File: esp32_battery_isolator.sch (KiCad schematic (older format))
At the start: 83 parts, among them J1 BATT1, J2 Conn_01x04_Female, J3 USB_B_Micro, J4 BATT2, J5 LOAD1, J6 CHGR, J7 LOAD2, J8 LOAD3, J9 Conn_01x03_Male, Q1 MMBT3904, Q10 AONR21321, Q11 AONR21321, Q12 MMBT3904, Q13 AONR21321, Q2 AONR21321, Q3 MMBT3904, Q4 AONR21321, Q5 MMBT3904, Q6 AONR21321, Q7 MMBT3904, Q8 AONR21321, Q9 MMBT3904, SW1 C492887, SW2 C492887, U1 ESP32-WROOM-32D, U2 XL1509_SOP8, U3 ADC128D818, U4 CC6903SO-30A, U5 CH340N, U6 CC6903SO-30A

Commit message: closer
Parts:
- removed Q13, Q6: AONR21321, Acea:DFN-TRANS_AONR21321, symbol Transistor_FET:QM6015D
- removed Q5: MMBT3904, Package_TO_SOT_SMD:SOT-23, symbol Transistor_BJT:MMBT3904
- removed R15: 200k, Resistor_SMD:R_0603_1608Metric, symbol Device:R_Small
- removed R25: 11k, Resistor_SMD:R_0603_1608Metric, symbol Device:R_Small
- removed R29: 510R, Resistor_SMD:R_0603_1608Metric, symbol Device:R_Small
- added BZ1: Buzzer, Buzzer_Beeper:SMDBuzzer_C201046, symbol Device:Buzzer
- Q10, Q11, Q2, Q4, Q8: value AONR21321 -> AONR21357
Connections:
- net B2C is gone; now on net COM: J9.1 (Pin_1), Q10.S, Q2.S, Q8.S, U6.3 (IP-), U6.4 (IP-)
- net B1VM: no longer R14.1
- net B2VM: no longer R16.1, R17.1, R20.1
- net COM: now also R14.1, R16.1, R17.1, R20.1
- net GND: now also BZ1.1 (-)
- net RST: now also U5.4 (~RTS)
- net BZR: now reaches U1.30 (IO18)
- net BZR: now also BZ1.2 (+)
- net B2ON: no longer names the net of U1.10 (IO25)
- no-connect marks 24 -> 23
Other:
- note added: "18V max."
- note added: "20A max cont.\n66A pulsed"
- note added: "25A max."
- note added: "2A max."
- note added: "3.4V max."
- note added: "Batt 2 connection (auxiliary)"
- note added: "Buzzer"
- note added: "CLRs?"
- note added: "Flyback?"
- note added: "Hold boot button to enter bootloader \nas ~RST~ will reset the uC automatically"
- note added: "Load 1 (freezer)"
- note added: "Load 2 (fridge)"
- note added: "Load 3 (lights)"
- note removed: "B1VM will only have 12v when B1 is \nconnected, threfore, B1’s MOSFETs will \nconduct without B1 attached."
- note removed: "B2VM will only have 12v when B2 is \nconnected, threfore, B2s MOSFETs will \nconduct without B2 attached."
- note removed: "Batt 2 isolator (auxiliary)"
- note removed: "Load 1 (fridge?)"
- note removed: "Load 2 (freezer?)"
- note removed: "Load 3 (lights?)"
- moved on the sheet: C10, C9, J1, J4, J6, Q1, Q11, Q4, R14, R27, R5, U4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

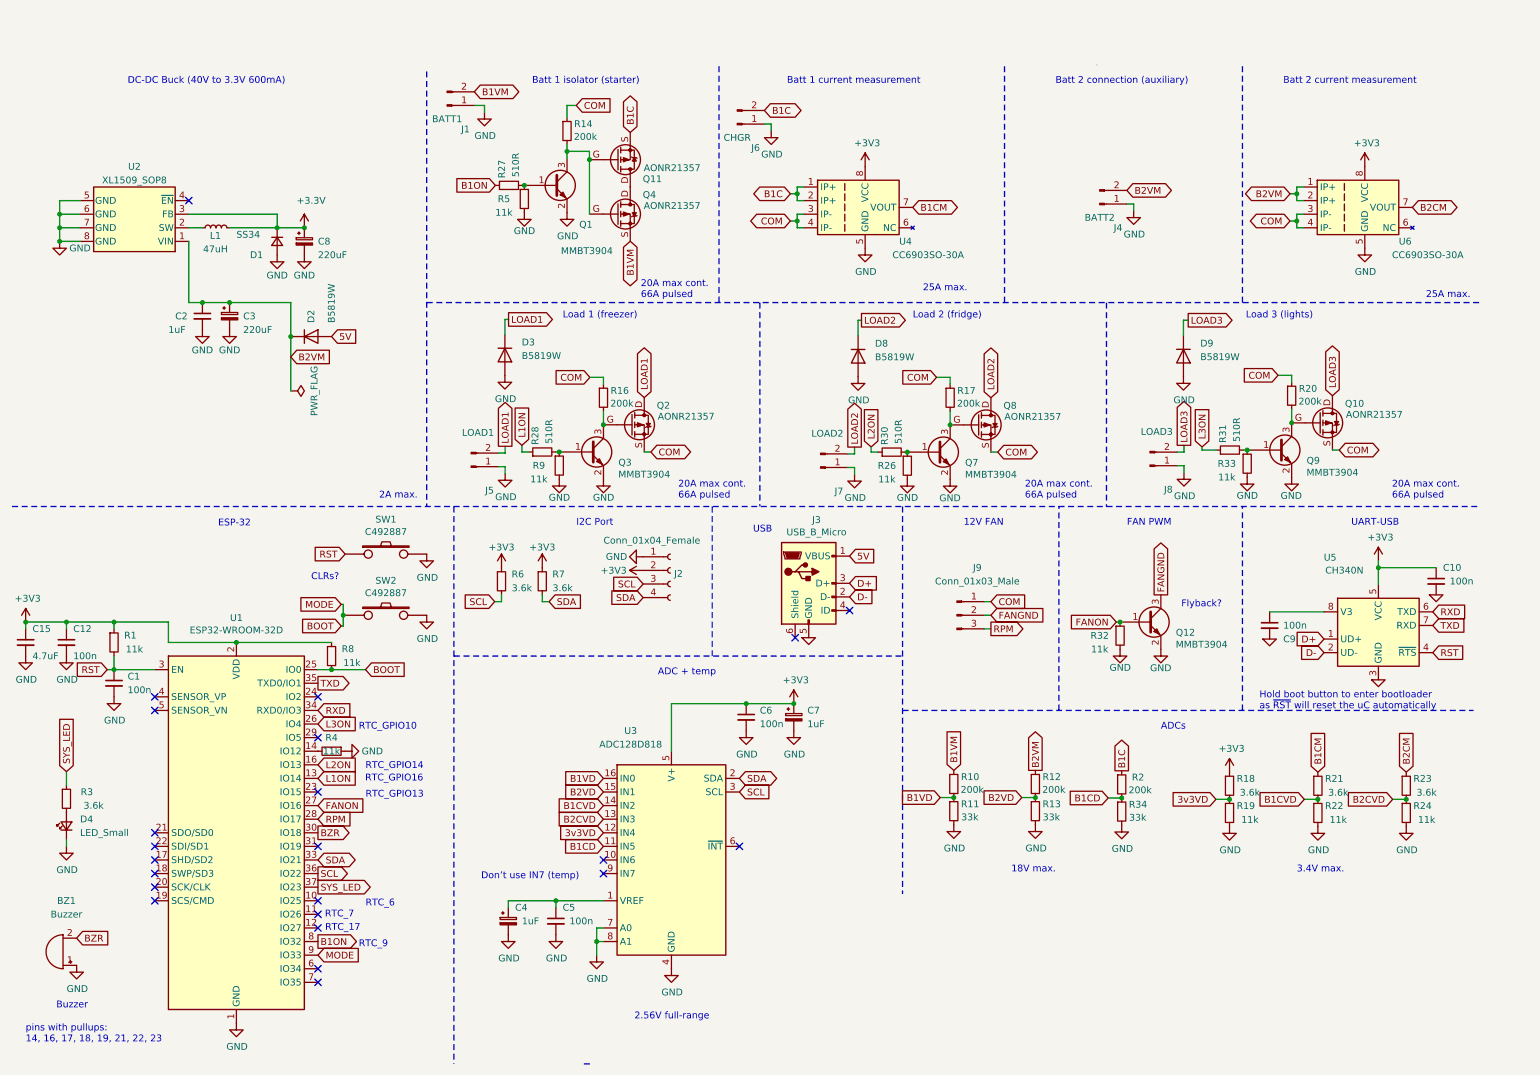
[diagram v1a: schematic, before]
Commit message: fixed daily couters not resetting
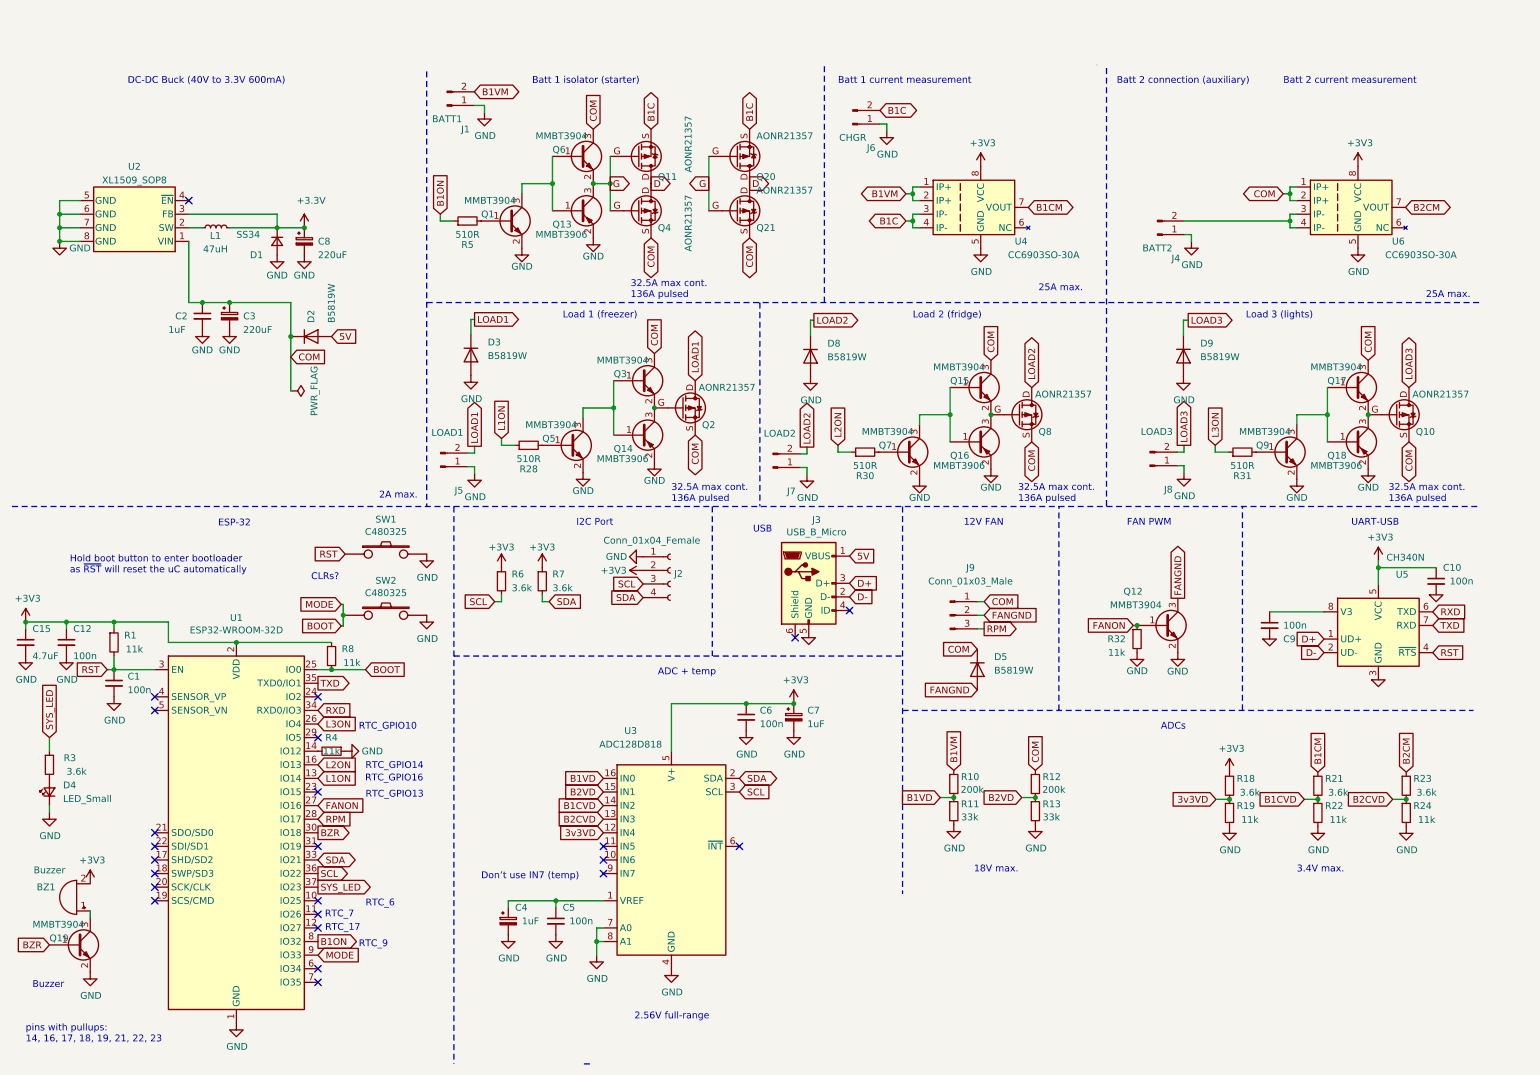
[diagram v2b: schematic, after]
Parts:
- removed R14, R16, R17, R2, R20: 200k, Resistor_SMD:R_0603_1608Metric, symbol Device:R_Small
- removed R26, R33, R9: 11k, Resistor_SMD:R_0603_1608Metric, symbol Device:R_Small
- removed R27: 510R, Resistor_SMD:R_0603_1608Metric, symbol Device:R_Small
- removed R34: 33k, Resistor_SMD:R_0603_1608Metric, symbol Device:R_Small
- added D5: B5819W, Diode_SMD:D_SOD-123, symbol Diode:1N4148WS
- added Q13, Q14, Q16, Q18: MMBT3906, Package_TO_SOT_SMD:SOT-23, symbol Transistor_BJT:MMBT3906
- added Q15, Q17, Q19, Q5, Q6: MMBT3904, Package_TO_SOT_SMD:SOT-23, symbol Transistor_BJT:MMBT3904
- added Q20, Q21: AONR21357, Acea:DFN-TRANS_AONR21321, symbol Transistor_FET:QM6015D
- R5: value 11k -> 510R; lcsc_part_number C25950 -> C269885; lcsc_url https://lcsc.com/product-detail/Chip-Resistor-Surface-Mount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 -> (none)
- SW1, SW2: value C492887 -> C480325; lcsc_part_number C492887 -> C480325; mfr_part_number TS-1091S-A5B3-C1D2 -> (none)
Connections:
- net +3V3: now also BZ1.2 (+)
- net B1C: now also U4.3 (IP-), U4.4 (IP-), Q20.S; no longer U4.1 (IP+), U4.2 (IP+)
- net B1ON: now also R5.1
- net B1VM: now also U4.1 (IP+), U4.2 (IP+); no longer Q4.S
- net BZR: now also Q19.1 (B); no longer BZ1.2 (+)
- net COM: now also C2.1, C3.1, D2.1 (K), Q3.3 (C), Q4.S, R12.1, U2.1 (VIN), U6.1 (IP+), U6.2 (IP+), D5.1 (K), Q15.3 (C), Q17.3 (C), Q21.S, Q6.3 (C); no longer U4.3 (IP-), U4.4 (IP-), U6.3 (IP-), U6.4 (IP-)
- net FANGND: now also D5.2 (A)
- net GND: now also Q13.2 (E), Q14.2 (E), Q16.2 (E), Q18.2 (E), Q19.2 (E), Q5.2 (E); no longer BZ1.1 (-), Q3.2 (E), R5.2
- net G: now reaches Q11.G, Q4.G
- net G: now also Q13.3 (C), Q20.G, Q21.G, Q6.2 (E); no longer Q1.3 (C)
- net at Q9.3 (C): now also Q17.1 (B), Q18.1 (B); no longer Q10.G
- net at Q7.3 (C): now also Q15.1 (B), Q16.1 (B); no longer Q8.G
- net at Q2.G: now also Q3.2 (E), Q14.3 (C); no longer Q3.3 (C)
- net at Q1.1 (B): now also R5.2; no longer R5.1
- net at Q3.1 (B): now also Q14.1 (B), Q5.3 (C); no longer R28.2
- net D: now reaches Q11.D, Q4.D
- net D: now also Q20.D, Q21.D
- net B1CD: no longer names the net of U3.11 (IN5)
- removed net B2VM: C2.1, C3.1, D2.1 (K), J4.2 (Pin_2), R12.1, U2.1 (VIN), U6.1 (IP+), U6.2 (IP+)
- new net: J4.2 (Pin_2), U6.3 (IP-), U6.4 (IP-)
- new net: BZ1.1 (-), Q19.3 (C)
- new net: Q1.3 (C), Q13.1 (B), Q6.1 (B)
- new net: Q5.1 (B), R28.2
- new net: Q15.2 (E), Q16.3 (C), Q8.G
- new net: Q10.G, Q17.2 (E), Q18.3 (C)
- no-connect marks 23 -> 24
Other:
- note added: "32.5A max cont.\n136A pulsed"
- note removed: "20A max cont.\n66A pulsed"
- note removed: "Flyback?"
- moved on the sheet: BZ1, D3, D4, D8, J4, J5, J6, J7, J9, Q12, Q2, Q3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
